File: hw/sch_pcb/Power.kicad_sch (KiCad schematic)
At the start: 52 parts, among them J3 HEADER_1x02, U10 TPS563249, U11 LTC3601, U12 NCP1117ST33, U9 LTC3601

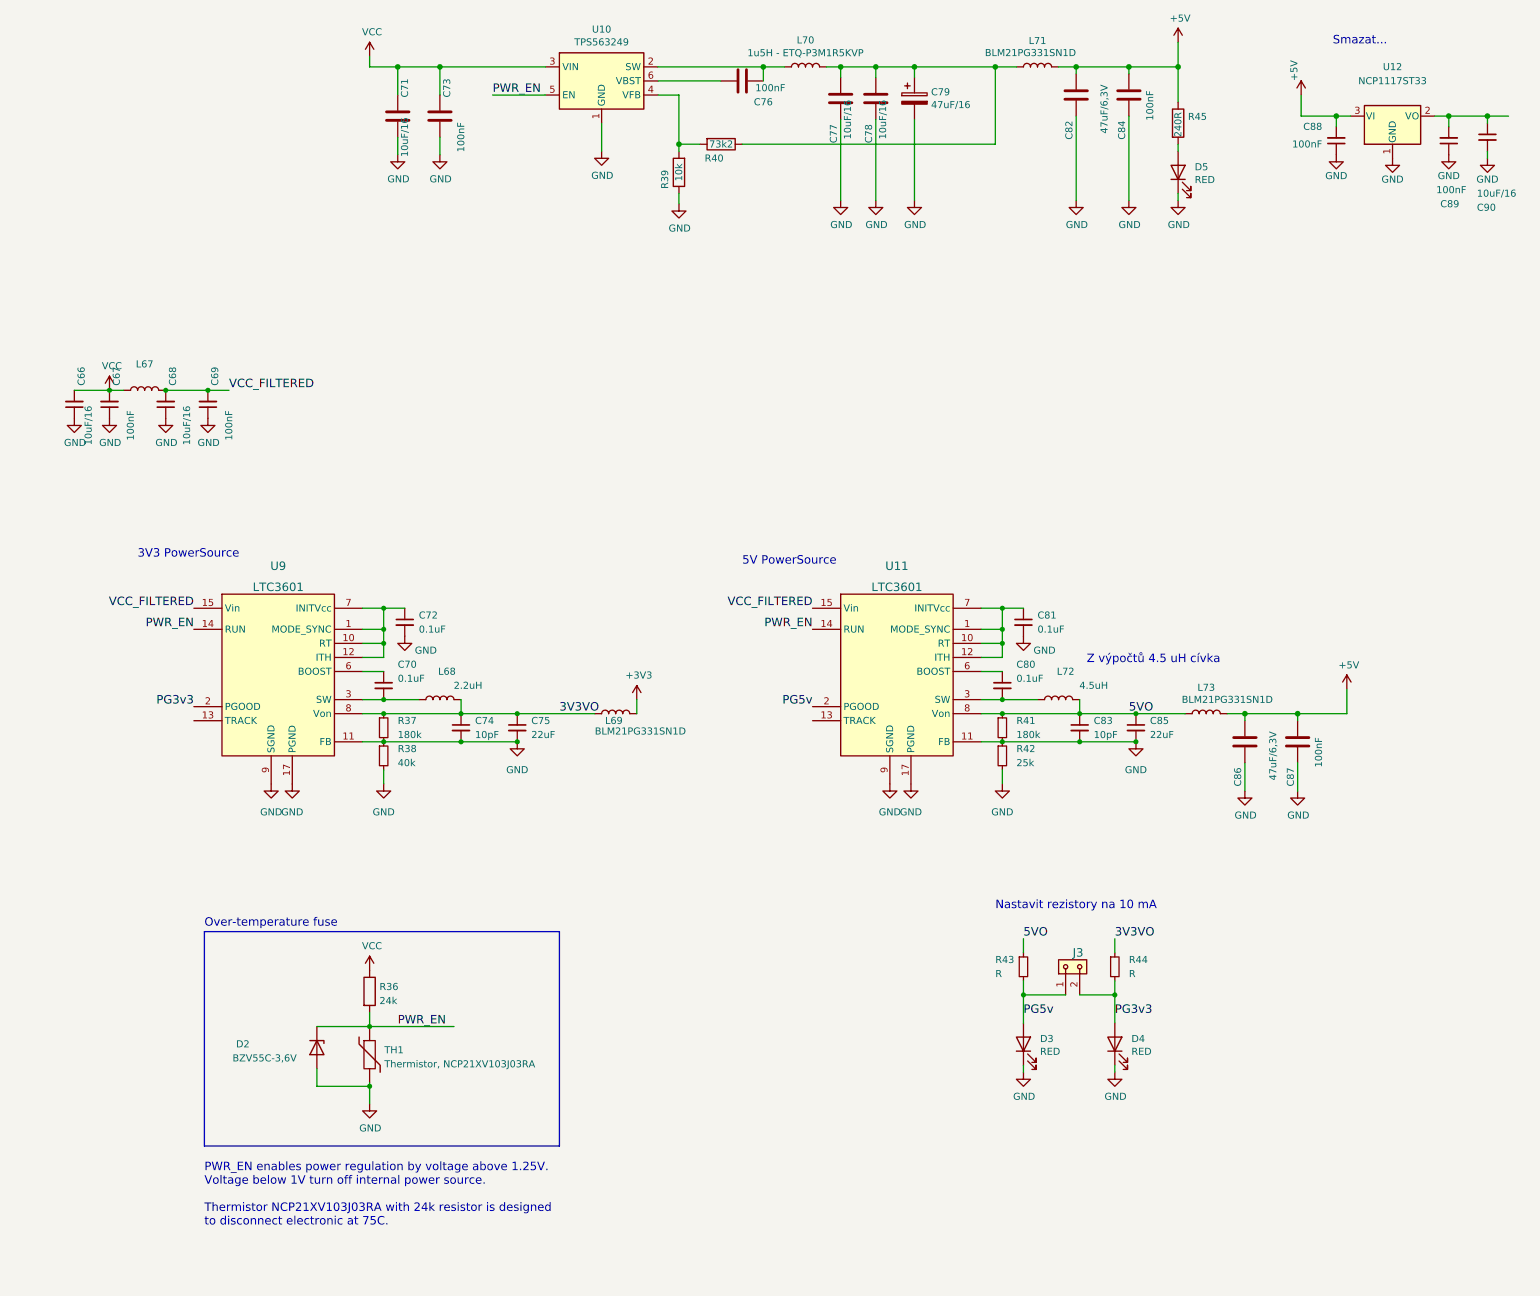
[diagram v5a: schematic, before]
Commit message: navrzeni soucastek regulatoru pro 5v #11
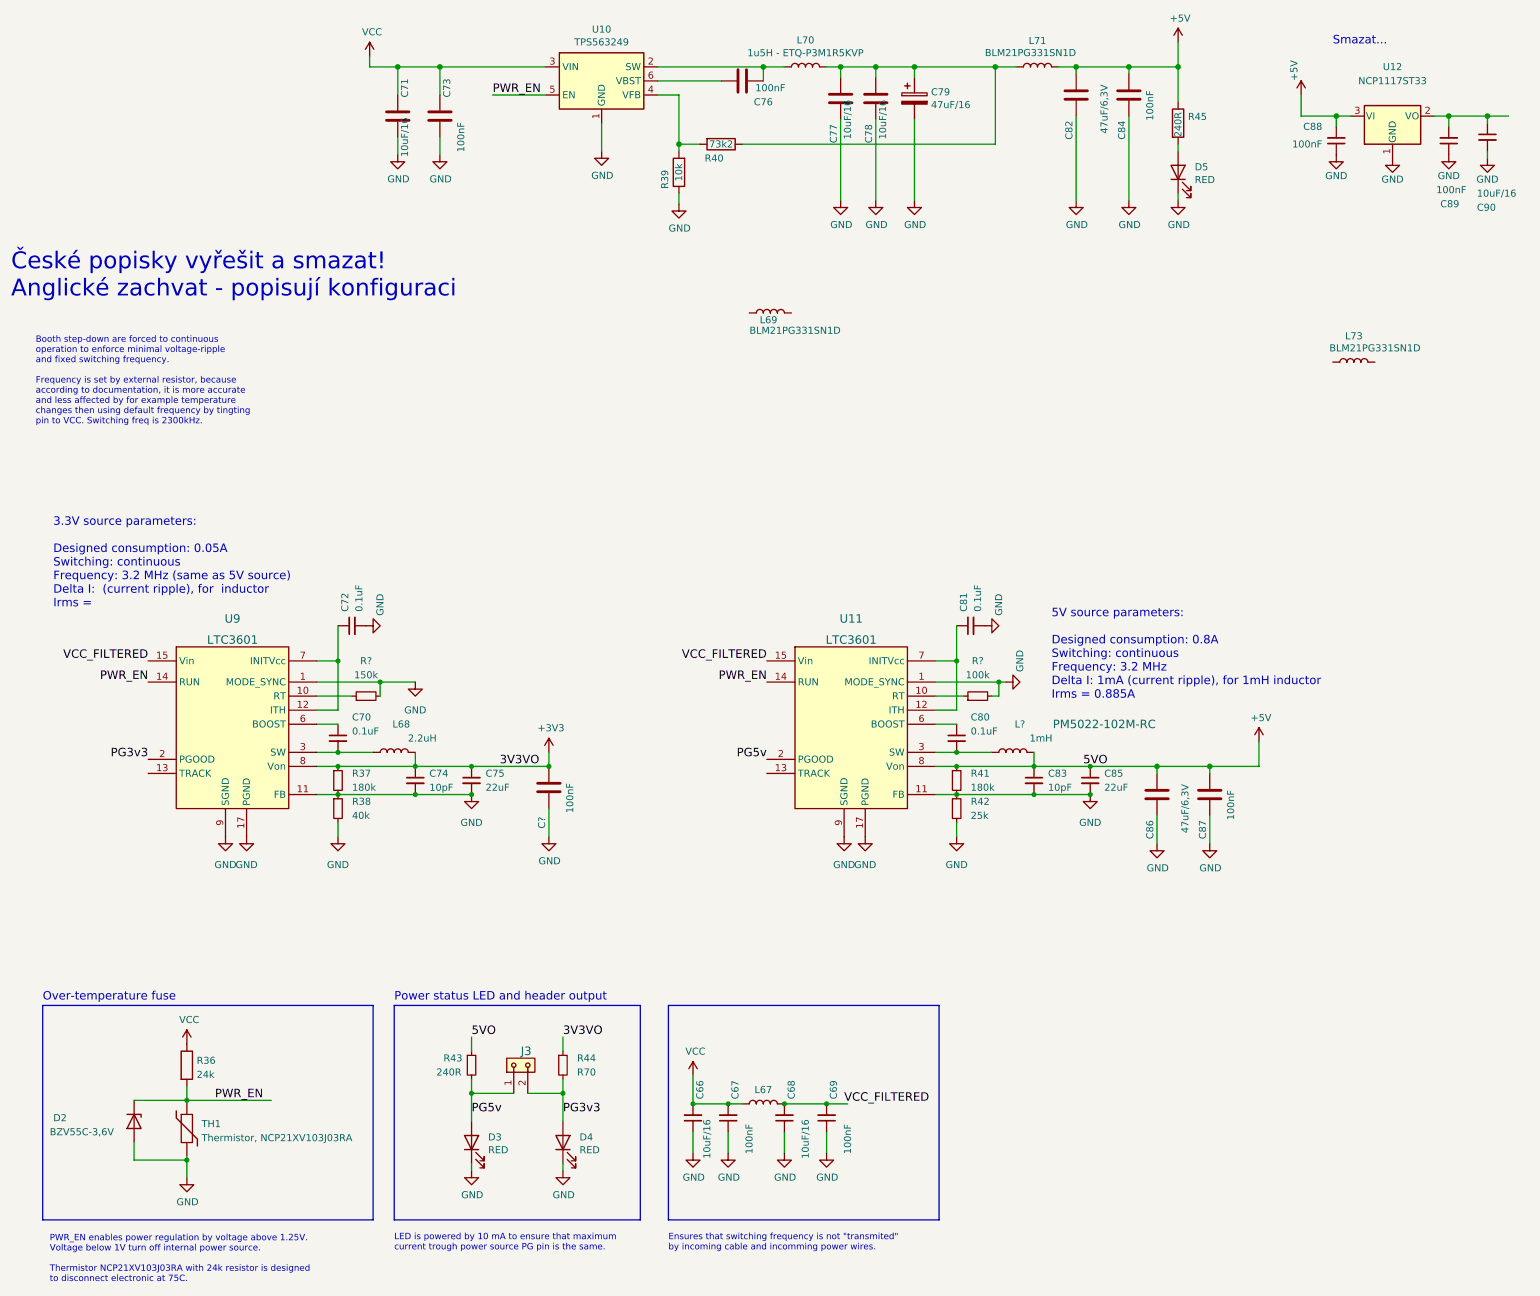
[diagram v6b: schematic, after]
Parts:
- removed L72: 4.5uH, symbol Device:L
- added C?: 100nF, Capacitor_SMD:C_0603_1608Metric, symbol Device:C
- added L?: 1mH, symbol Device:L
- added R?: 100k, symbol Device:R_Small
- added R?: 150k, symbol Device:R_Small
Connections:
- net +3V3: now also C74.1, C75.1, L68.2, R37.1, R44.1, U9.8 (Von), C?.2; no longer L69.2
- net +5V: now also C83.1, C85.1, R41.1, R43.1, U11.8 (Von), L?.2; no longer L73.2
- net GND: now also U11.1 (MODE_SYNC), U9.1 (MODE_SYNC), C?.1, R?.2, R?.2
- net at C72.1, U9.12 (ITH), U9.7 (INITVcc): no longer U9.1 (MODE_SYNC), U9.10 (RT)
- net at C80.2, U11.3 (SW), U11.4 (SW): now also L?.1
- net at C81.1, U11.12 (ITH), U11.7 (INITVcc): no longer U11.1 (MODE_SYNC), U11.10 (RT)
- removed net 3V3VO: C74.1, C75.1, L68.2, L69.1, R37.1, R44.1, U9.8 (Von)
- removed net 5VO: C83.1, C85.1, L73.1, R41.1, R43.1, U11.8 (Von)
- new net: R?.1, U11.10 (RT)
- new net: R?.1, U9.10 (RT)
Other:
- note added: "3.3V source parameters: Designed consumption: 0.05A Switching: continuous Frequency: 3.2 MHz (same as 5V source) Delta I: (current ripple), for inductor Irms ="
- note added: "5V source parameters: Designed consumption: 0.8A Switching: continuous Frequency: 3.2 MHz Delta I: 1mA (current ripple), for 1mH inductor Irms = 0.885A"
- note added: "Booth step-down are forced to continuous operation to enforce minimal voltage-ripple and fixed switching frequency. Frequency is set by external resistor, because according to documentation, it is more accurate and less affected by for example temperature changes then using default frequency by tingting pin to VCC. Switching freq is 2300kHz."
- note added: "Ensures that switching frequency is not "transmited" by incoming cable and incomming power wires."
- note added: "LED is powered by 10 mA to ensure that maximum current trough power source PG pin is the same."
- note added: "Power status LED and header output"
- note added: "České popisky vyřešit a smazat! Anglické zachvat - popisují konfiguraci"
- note removed: "3V3 PowerSource"
- note removed: "5V PowerSource"
- note removed: "Nastavit rezistory na 10 mA"
- note removed: "Z výpočtů 4.5 uH cívka"
- moved on the sheet: C66, C67, C68, C69, C70, C72, C74, C75, C80, C81, C83, C85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

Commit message: Pridani novych otvoru pro sloupky pro montaz anteny #20, WIP
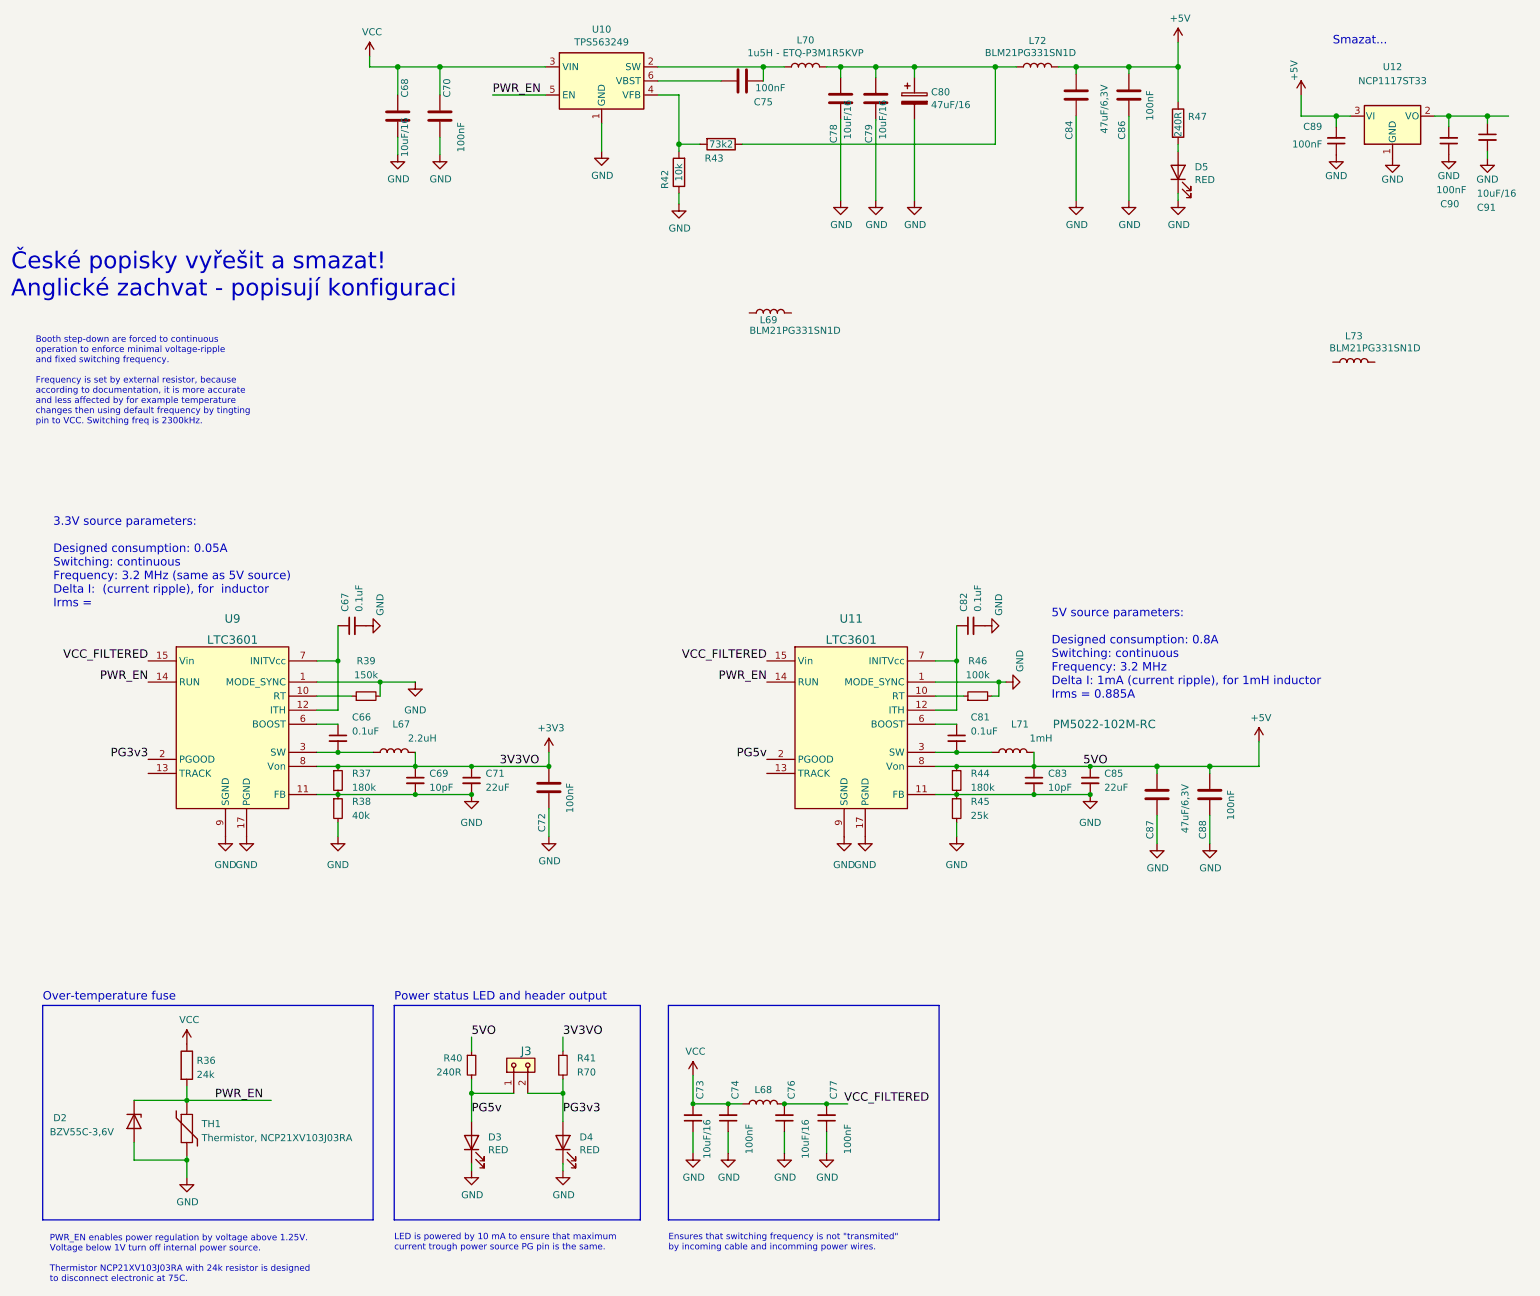
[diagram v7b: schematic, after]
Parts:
- gave numbers to parts that had none: 4
- renumbered C70 to C66, C72 to C67, C71 to C68, C74 to C69, C73 to C70, C75 to C71, C66 to C73, C67 to C74, C76 to C75, C68 to C76, C69 to C77, C77 to C78, C78 to C79, C79 to C80, C80 to C81, C81 to C82, C82 to C84, C84 to C86, C86 to C87, C87 to C88, C88 to C89, C89 to C90, C90 to C91, L68 to L67, L67 to L68, L71 to L72, R43 to R40, R44 to R41, R39 to R42, R40 to R43, R41 to R44, R42 to R45, R45 to R47

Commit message: Cleanup title block update assets submodule.
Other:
- title: (none) -> QFHMIX01D
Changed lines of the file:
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@@
 (kicad_sch (version 20211123) (generator eeschema)
   (paper "A4")
+  (title_block
+    (title "QFHMIX01D")
+    (date "2021-04-21")
+    (comment 2 "Frontend for QFH active antenna")
+  )
   (junction (at 133.35 -17.78) (diameter 1.016) (color 0 0 0 0)
   )
